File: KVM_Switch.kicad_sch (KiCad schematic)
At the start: 0 parts

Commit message: Updated library structure
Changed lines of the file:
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@@
 	(wire
 		(pts
-			(xy 101.6 69.85) (xy 99.06 69.85)
+			(xy 99.06 88.9) (xy 99.06 69.85)
 		)
 		(stroke
@@
 	(wire
 		(pts
+			(xy 139.7 104.14) (xy 152.4 104.14)
+		)
+		(stroke
+			(width 0)
+			(type default)
+		)
+	)
+	(wire
+		(pts
 			(xy 99.06 88.9) (xy 99.06 109.22)
 		)
@@
 	(wire
 		(pts
-			(xy 139.7 104.14) (xy 152.4 104.14)
+			(xy 99.06 69.85) (xy 101.6 69.85)
 		)
 		(stroke
@@
 		)
 	)
-	(wire
-		(pts
-			(xy 99.06 69.85) (xy 99.06 88.9)
-		)
-		(stroke
-			(width 0)
-			(type default)
+	(label "SW"
+		(at 99.06 88.9 180)
+		(effects
+			(font
+				(size 1.27 1.27)
+			)
+			(justify right bottom)
 		)
 	)

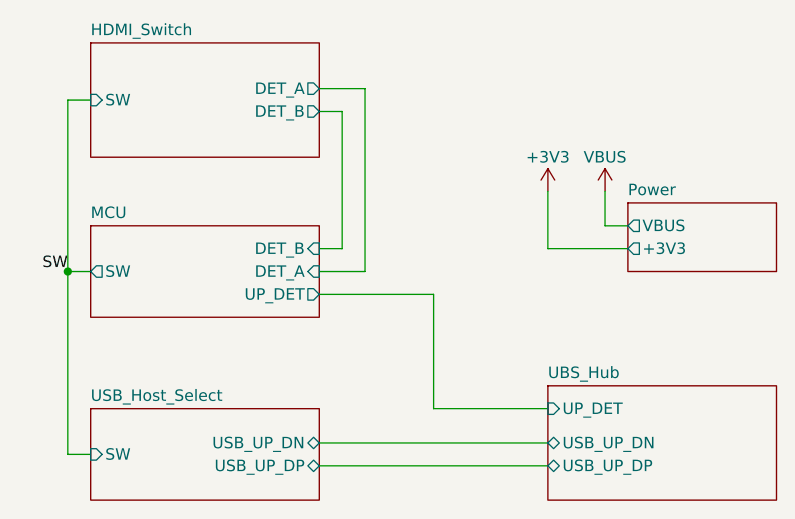
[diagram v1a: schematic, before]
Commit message: Library and Schematics Fixes
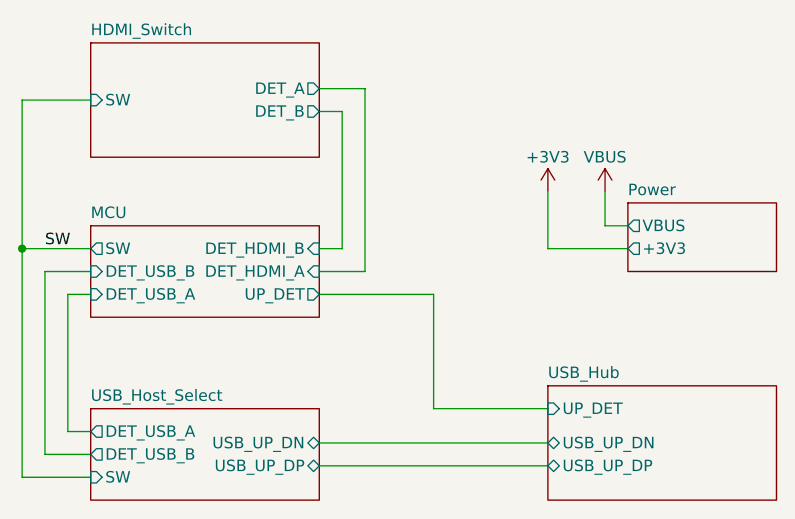
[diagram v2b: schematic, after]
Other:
- sheet UBS_Hub renamed USB_Hub
- sheet MCU ports: added DET_HDMI_A, DET_HDMI_B, DET_USB_A, DET_USB_B; removed DET_A, DET_B
- sheet USB_Host_Select ports: added DET_USB_A, DET_USB_B; removed none
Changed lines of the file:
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@@
 	)
 	(junction
-		(at 99.06 88.9)
+		(at 93.98 86.36)
 		(diameter 0)
 		(color 0 0 0 0)
@@
 	(wire
 		(pts
-			(xy 99.06 88.9) (xy 99.06 69.85)
-		)
-		(stroke
-			(width 0)
-			(type default)
-		)
-	)
-	(wire
-		(pts
 			(xy 152.4 80.01) (xy 152.4 86.36)
 		)
@@
 	(wire
 		(pts
+			(xy 101.6 91.44) (xy 99.06 91.44)
+		)
+		(stroke
+			(width 0)
+			(type default)
+		)
+	)
+	(wire
+		(pts
 			(xy 127 110.49) (xy 152.4 110.49)
 		)
@@
 	(wire
 		(pts
+			(xy 93.98 86.36) (xy 93.98 111.76)
+		)
+		(stroke
+			(width 0)
+			(type default)
+		)
+	)
+	(wire
+		(pts
+			(xy 101.6 109.22) (xy 96.52 109.22)
+		)
+		(stroke
+			(width 0)
+			(type default)
+		)
+	)
+	(wire
+		(pts
+			(xy 99.06 106.68) (xy 101.6 106.68)
+		)
+		(stroke
+			(width 0)
+			(type default)
+		)
+	)
+	(wire
+		(pts
 			(xy 139.7 91.44) (xy 139.7 104.14)
 		)
@@
 	(wire
 		(pts
-			(xy 99.06 88.9) (xy 99.06 109.22)
-		)
-		(stroke
-			(width 0)
-			(type default)
-		)
-	)
-	(wire
-		(pts
-			(xy 99.06 69.85) (xy 101.6 69.85)
-		)
-		(stroke
-			(width 0)
-			(type default)
-		)
-	)
-	(wire
-		(pts
-			(xy 99.06 109.22) (xy 101.6 109.22)
+			(xy 93.98 69.85) (xy 101.6 69.85)
+		)
+		(stroke
+			(width 0)
+			(type default)
+		)
+	)
+	(wire
+		(pts
+			(xy 93.98 111.76) (xy 101.6 111.76)
+		)
+		(stroke
+			(width 0)
+			(type default)
+		)
+	)
+	(wire
+		(pts
+			(xy 93.98 69.85) (xy 93.98 86.36)
 		)
 		(stroke
@@
 	(wire
 		(pts
-			(xy 99.06 88.9) (xy 101.6 88.9)
+			(xy 96.52 109.22) (xy 96.52 88.9)
+		)
+		(stroke
+			(width 0)
+			(type default)
+		)
+	)
+	(wire
+		(pts
+			(xy 96.52 88.9) (xy 101.6 88.9)
 		)
 		(stroke
@@
 	(wire
 		(pts
+			(xy 93.98 86.36) (xy 101.6 86.36)
+		)
+		(stroke
+			(width 0)
+			(type default)
+		)
+	)
+	(wire
+		(pts
 			(xy 127 68.58) (xy 132.08 68.58)
 		)
@@
 	(wire
 		(pts
+			(xy 99.06 91.44) (xy 99.06 106.68)
+		)
+		(stroke
+			(width 0)
+			(type default)
+		)
+	)
+	(wire
+		(pts
 			(xy 152.4 86.36) (xy 161.29 86.36)
 		)
@@
 	)
 	(label "SW"
-		(at 99.06 88.9 180)
+		(at 96.52 86.36 0)
 		(effects
 			(font
 				(size 1.27 1.27)
 			)
-			(justify right bottom)
+			(justify left bottom)
 		)
 	)
@@
 			(color 255 255 194 1)
 		)
-		(property "Sheetname" "UBS_Hub"
+		(property "Sheetname" "USB_Hub"
 			(at 152.4 100.8884 0)
 			(show_name no)
@@
 		)
 		(pin "SW" input
-			(at 101.6 109.22 180)
+			(at 101.6 111.76 180)
 			(effects
 				(font
@@
 				)
 				(justify right)
+			)
+		)
+		(pin "DET_USB_A" output
+			(at 101.6 106.68 180)
+			(effects
+				(font
+					(size 1.27 1.27)
+				)
+				(justify left)
+			)
+		)
+		(pin "DET_USB_B" output
+			(at 101.6 109.22 180)
+			(effects
+				(font
+					(size 1.27 1.27)
+				)
+				(justify left)
 			)
 		)
@@
 		)
 		(pin "SW" output
-			(at 101.6 88.9 180)
-			(effects
-				(font
-					(size 1.27 1.27)
-				)
-				(justify left)
-			)
-		)
-		(pin "DET_A" input
-			(at 127 88.9 0)
-			(effects
-				(font
-					(size 1.27 1.27)
-				)
-				(justify right)
-			)
-		)
-		(pin "DET_B" input
-			(at 127 86.36 0)
-			(effects
-				(font
-					(size 1.27 1.27)
-				)
-				(justify right)
+			(at 101.6 86.36 180)
+			(effects
+				(font
+					(size 1.27 1.27)
+				)
+				(justify left)
 			)
 		)
@@
 			)
 		)
+		(pin "DET_HDMI_A" input
+			(at 127 88.9 0)
+			(effects
+				(font
+					(size 1.27 1.27)
+				)
+				(justify right)
+			)
+		)
+		(pin "DET_HDMI_B" input
+			(at 127 86.36 0)
+			(effects
+				(font
+					(size 1.27 1.27)
+				)
+				(justify right)
+			)
+		)
+		(pin "DET_USB_A" input
+			(at 101.6 91.44 180)
+			(effects
+				(font
+					(size 1.27 1.27)
+				)
+				(justify left)
+			)
+		)
+		(pin "DET_USB_B" input
+			(at 101.6 88.9 180)
+			(effects
+				(font
+					(size 1.27 1.27)
+				)
+				(justify left)
+			)
+		)

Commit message: More schematics fixes & Layout attempt
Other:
- sheet MCU ports: added HDMI_SW, USB_SW; removed SW
- company: (none) -> Stanisław Basiuk
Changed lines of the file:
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@@
 	(title_block
 		(title "KVM_Switch")
-		(date "2026-08-23")
+		(date "2026-09-07")
 		(rev "A")
-	)
-	(junction
-		(at 93.98 86.36)
-		(diameter 0)
-		(color 0 0 0 0)
+		(company "Stanisław Basiuk")
 	)
 	(wire
@@
 	(wire
 		(pts
-			(xy 101.6 91.44) (xy 99.06 91.44)
+			(xy 101.6 92.71) (xy 99.06 92.71)
 		)
 		(stroke
@@
 	(wire
 		(pts
-			(xy 93.98 86.36) (xy 93.98 111.76)
+			(xy 101.6 85.09) (xy 99.06 85.09)
 		)
 		(stroke
@@
 	(wire
 		(pts
+			(xy 93.98 87.63) (xy 93.98 111.76)
+		)
+		(stroke
+			(width 0)
+			(type default)
+		)
+	)
+	(wire
+		(pts
 			(xy 139.7 104.14) (xy 152.4 104.14)
 		)
@@
 	(wire
 		(pts
-			(xy 93.98 69.85) (xy 101.6 69.85)
+			(xy 101.6 87.63) (xy 93.98 87.63)
+		)
+		(stroke
+			(width 0)
+			(type default)
+		)
+	)
+	(wire
+		(pts
+			(xy 99.06 69.85) (xy 101.6 69.85)
+		)
+		(stroke
+			(width 0)
+			(type default)
+		)
+	)
+	(wire
+		(pts
+			(xy 99.06 85.09) (xy 99.06 69.85)
 		)
 		(stroke
@@
 	(wire
 		(pts
-			(xy 93.98 69.85) (xy 93.98 86.36)
-		)
-		(stroke
-			(width 0)
-			(type default)
-		)
-	)
-	(wire
-		(pts
 			(xy 127 86.36) (xy 129.54 86.36)
 		)
@@
 	(wire
 		(pts
-			(xy 96.52 109.22) (xy 96.52 88.9)
-		)
-		(stroke
-			(width 0)
-			(type default)
-		)
-	)
-	(wire
-		(pts
-			(xy 96.52 88.9) (xy 101.6 88.9)
+			(xy 96.52 109.22) (xy 96.52 90.17)
+		)
+		(stroke
+			(width 0)
+			(type default)
+		)
+	)
+	(wire
+		(pts
+			(xy 96.52 90.17) (xy 101.6 90.17)
 		)
 		(stroke
@@
 	(wire
 		(pts
-			(xy 93.98 86.36) (xy 101.6 86.36)
-		)
-		(stroke
-			(width 0)
-			(type default)
-		)
-	)
-	(wire
-		(pts
 			(xy 127 68.58) (xy 132.08 68.58)
 		)
@@
 	(wire
 		(pts
-			(xy 99.06 91.44) (xy 99.06 106.68)
+			(xy 99.06 92.71) (xy 99.06 106.68)
 		)
 		(stroke
@@
 			(width 0)
 			(type default)
-		)
-	)
-	(label "SW"
-		(at 96.52 86.36 0)
-		(effects
-			(font
-				(size 1.27 1.27)
-			)
-			(justify left bottom)
 		)
 	)
@@
 		(in_pos_files yes)
 		(dnp no)
-		(property "Reference" "#PWR049"
+		(property "Reference" "#PWR056"
 			(at 152.4 83.82 0)
 			(hide yes)
@@
 			(project "KVM_Switch"
 				(path "/94386106-ccd4-487f-b5c5-d52ec3dd59db"
-					(reference "#PWR049")
+					(reference "#PWR056")
 					(unit 1)
 				)
@@
 		(in_pos_files yes)
 		(dnp no)
-		(property "Reference" "#PWR050"
+		(property "Reference" "#PWR057"
 			(at 158.75 83.82 0)
 			(hide yes)
@@
 			(project "KVM_Switch"
 				(path "/94386106-ccd4-487f-b5c5-d52ec3dd59db"
-					(reference "#PWR050")
+					(reference "#PWR057")
 					(unit 1)
 				)
@@
 			)
 		)
-		(pin "SW" output
-			(at 101.6 86.36 180)
-			(effects
-				(font
-					(size 1.27 1.27)
-				)
-				(justify left)
-			)
-		)
 		(pin "UP_DET" output
 			(at 127 91.44 0)
@@
 		)
 		(pin "DET_USB_A" input
-			(at 101.6 91.44 180)
+			(at 101.6 92.71 180)
 			(effects
 				(font
@@
 		)
 		(pin "DET_USB_B" input
-			(at 101.6 88.9 180)
-			(effects
-				(font
+			(at 101.6 90.17 180)
+			(effects
+				(font
+					(size 1.27 1.27)
+				)
+				(justify left)
+			)
+		)
+		(pin "HDMI_SW" output
+			(at 101.6 85.09 180)
+			(effects
+				(font
+					(size 1.27 1.27)
+				)
+				(justify left)
+			)
+		)
+		(pin "USB_SW" output
+			(at 101.6 87.63 180)
+			(effects
+				(font
